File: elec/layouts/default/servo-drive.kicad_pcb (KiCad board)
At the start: 4 copper layers, 46 x 42.3 mm, 108 parts

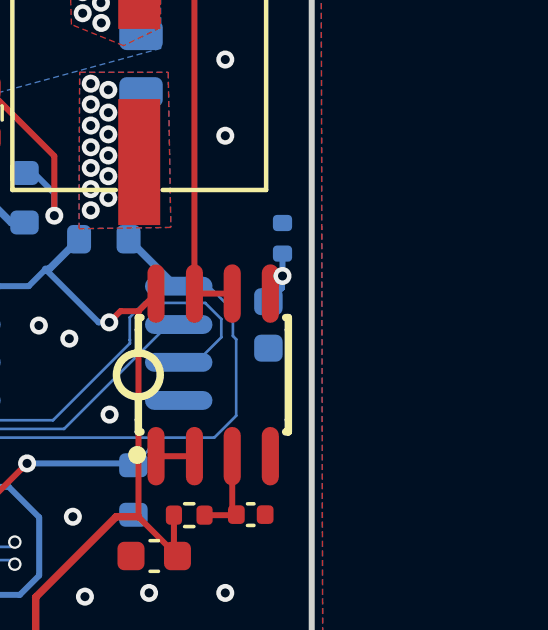
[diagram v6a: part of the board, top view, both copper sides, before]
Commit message: Upgrade default layout paths
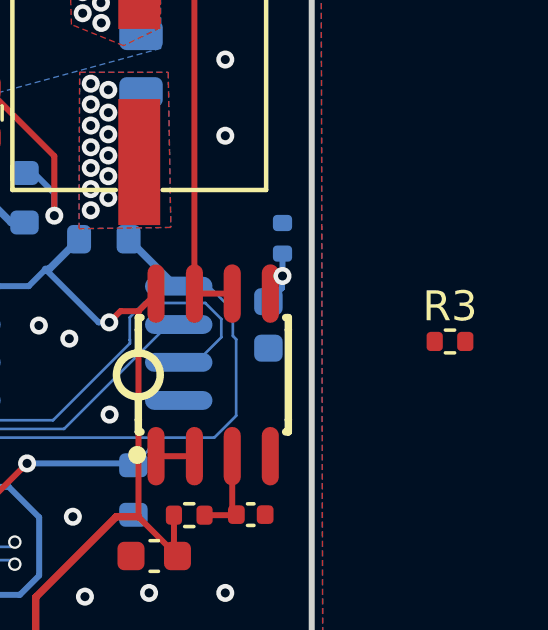
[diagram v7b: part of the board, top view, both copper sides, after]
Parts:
- added R3: 10kOhm, Resistor_SMD:R_0402_1005Metric, F.Cu at (177.7, 103.4)
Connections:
- net servo_drive.ato/ServoDrive.gnd renamed servo_drive.ato:ServoDrive.gnd
- net servo_drive.ato/ServoDrive.micro_kit/usb_dm-usb/dm renamed servo_drive.ato:ServoDrive.micro_kit.usb_dm-usb.dm
- net servo_drive.ato/ServoDrive.micro_kit/usb_dp-usb/dp renamed servo_drive.ato:ServoDrive.micro_kit.usb_dp-usb.dp
- net servo_drive.ato/ServoDrive.position_sensor/scl renamed servo_drive.ato:ServoDrive.position_sensor.scl
- net servo_drive.ato/ServoDrive.position_sensor/sda renamed servo_drive.ato:ServoDrive.position_sensor.sda
- net servo_drive.ato/ServoDrive.power_stage/high_in_a renamed servo_drive.ato:ServoDrive.power_stage.high_in_a
- net servo_drive.ato/ServoDrive.power_stage/high_in_b renamed servo_drive.ato:ServoDrive.power_stage.high_in_b
- net servo_drive.ato/ServoDrive.power_stage/high_in_c renamed servo_drive.ato:ServoDrive.power_stage.high_in_c
- net servo_drive.ato/ServoDrive.power_stage/i_fb_a renamed servo_drive.ato:ServoDrive.power_stage.i_fb_a
- net servo_drive.ato/ServoDrive.power_stage/i_fb_b renamed servo_drive.ato:ServoDrive.power_stage.i_fb_b
- net servo_drive.ato/ServoDrive.power_stage/i_fb_c renamed servo_drive.ato:ServoDrive.power_stage.i_fb_c
- net servo_drive.ato/ServoDrive.power_stage/low_in_a renamed servo_drive.ato:ServoDrive.power_stage.low_in_a
- net servo_drive.ato/ServoDrive.power_stage/low_in_b renamed servo_drive.ato:ServoDrive.power_stage.low_in_b
- net servo_drive.ato/ServoDrive.power_stage/low_in_c renamed servo_drive.ato:ServoDrive.power_stage.low_in_c
- net servo_drive.ato/ServoDrive.power_stage/out_a renamed servo_drive.ato:ServoDrive.power_stage.out_a
- net servo_drive.ato/ServoDrive.power_stage/out_b renamed servo_drive.ato:ServoDrive.power_stage.out_b
- net servo_drive.ato/ServoDrive.power_stage/out_c renamed servo_drive.ato:ServoDrive.power_stage.out_c
- net servo_drive.ato/ServoDrive.usb/cc1 renamed servo_drive.ato:ServoDrive.usb.cc1
- net servo_drive.ato/ServoDrive.usb/cc2 renamed servo_drive.ato:ServoDrive.usb.cc2
- net servo_drive.ato/ServoDrive.usb/vbus-usb_diode/anode renamed servo_drive.ato:ServoDrive.usb.vbus-usb_diode.anode
- net servo_drive.ato/ServoDrive.v_10 renamed servo_drive.ato:ServoDrive.v_10
- net servo_drive.ato/ServoDrive.v_3 renamed servo_drive.ato:ServoDrive.v_3
- net servo_drive.ato/ServoDrive.vbatt renamed servo_drive.ato:ServoDrive.vbatt
- net servo_drive.ato/ServoDrive.voltage_input_vdiv/out renamed servo_drive.ato:ServoDrive.voltage_input_vdiv.out
- net servo_drive.ato/ServoDrive/buck.SGND renamed servo_drive.ato:ServoDrive.buck.SGND
- net servo_drive.ato/ServoDrive/buck.buck_converter/BST renamed servo_drive.ato:ServoDrive.buck.buck_converter.BST
- net servo_drive.ato/ServoDrive/buck.buck_converter/FB-fb_vdiv/output renamed servo_drive.ato:ServoDrive.buck.buck_converter.FB-fb_vdiv.output
- net servo_drive.ato/ServoDrive/buck.buck_converter/LX renamed servo_drive.ato:ServoDrive.buck.buck_converter.LX
- net servo_drive.ato/ServoDrive/buck.buck_converter/SS renamed servo_drive.ato:ServoDrive.buck.buck_converter.SS
- net servo_drive.ato/ServoDrive/buck.buck_converter/VCC renamed servo_drive.ato:ServoDrive.buck.buck_converter.VCC
- net servo_drive.ato/ServoDrive/buck/buck_converter.CF renamed servo_drive.ato:ServoDrive.buck.buck_converter.CF
- net servo_drive.ato/ServoDrive/buck/buck_converter.RESET renamed servo_drive.ato:ServoDrive.buck.buck_converter.RESET
- net servo_drive.ato/ServoDrive/buck/buck_converter.RT renamed servo_drive.ato:ServoDrive.buck.buck_converter.RT
- net servo_drive.ato/ServoDrive/buck/buck_converter.SYNC renamed servo_drive.ato:ServoDrive.buck.buck_converter.SYNC
- net servo_drive.ato/ServoDrive/ldo.ldo_ic/bypass renamed servo_drive.ato:ServoDrive.ldo.ldo_ic.bypass
- net servo_drive.ato/ServoDrive/micro_kit.boot_vdiv/output-flash/ncs-micro/qspi_ss_n renamed servo_drive.ato:ServoDrive.micro_kit.boot_vdiv.output-flash.ncs-micro.qspi_ss_n
- net servo_drive.ato/ServoDrive/micro_kit.flash/clk-micro/qspi_sclk renamed servo_drive.ato:ServoDrive.micro_kit.flash.clk-micro.qspi_sclk
- net servo_drive.ato/ServoDrive/micro_kit.flash/di-micro/qspi_sd0 renamed servo_drive.ato:ServoDrive.micro_kit.flash.di-micro.qspi_sd0
- net servo_drive.ato/ServoDrive/micro_kit.flash/do-micro/qspi_sd1 renamed servo_drive.ato:ServoDrive.micro_kit.flash.do-micro.qspi_sd1
- net servo_drive.ato/ServoDrive/micro_kit.flash/io2-micro/qspi_sd2 renamed servo_drive.ato:ServoDrive.micro_kit.flash.io2-micro.qspi_sd2
- net servo_drive.ato/ServoDrive/micro_kit.flash/io3-micro/qspi_sd3 renamed servo_drive.ato:ServoDrive.micro_kit.flash.io3-micro.qspi_sd3
- net servo_drive.ato/ServoDrive/micro_kit.micro/dvdd-micro/vreg_vout renamed servo_drive.ato:ServoDrive.micro_kit.micro.dvdd-micro.vreg_vout
- net servo_drive.ato/ServoDrive/micro_kit.micro/run renamed servo_drive.ato:ServoDrive.micro_kit.micro.run
- net servo_drive.ato/ServoDrive/micro_kit.micro/usb_dm renamed servo_drive.ato:ServoDrive.micro_kit.micro.usb_dm
- net servo_drive.ato/ServoDrive/micro_kit.micro/usb_dp renamed servo_drive.ato:ServoDrive.micro_kit.micro.usb_dp
- net servo_drive.ato/ServoDrive/micro_kit.micro/xin-osc/in renamed servo_drive.ato:ServoDrive.micro_kit.micro.xin-osc.in
- net servo_drive.ato/ServoDrive/micro_kit.micro/xout renamed servo_drive.ato:ServoDrive.micro_kit.micro.xout
- net servo_drive.ato/ServoDrive/micro_kit.osc/out renamed servo_drive.ato:ServoDrive.micro_kit.osc.out
- net servo_drive.ato/ServoDrive/micro_kit/micro.gpio10 renamed servo_drive.ato:ServoDrive.micro_kit.micro.gpio10
- net servo_drive.ato/ServoDrive/micro_kit/micro.gpio11 renamed servo_drive.ato:ServoDrive.micro_kit.micro.gpio11
- net servo_drive.ato/ServoDrive/micro_kit/micro.gpio12 renamed servo_drive.ato:ServoDrive.micro_kit.micro.gpio12
- net servo_drive.ato/ServoDrive/micro_kit/micro.gpio13 renamed servo_drive.ato:ServoDrive.micro_kit.micro.gpio13
- net servo_drive.ato/ServoDrive/micro_kit/micro.gpio14 renamed servo_drive.ato:ServoDrive.micro_kit.micro.gpio14
- net servo_drive.ato/ServoDrive/micro_kit/micro.gpio15 renamed servo_drive.ato:ServoDrive.micro_kit.micro.gpio15
- net servo_drive.ato/ServoDrive/micro_kit/micro.gpio16 renamed servo_drive.ato:ServoDrive.micro_kit.micro.gpio16
- net servo_drive.ato/ServoDrive/micro_kit/micro.gpio17 renamed servo_drive.ato:ServoDrive.micro_kit.micro.gpio17
- net servo_drive.ato/ServoDrive/micro_kit/micro.gpio18 renamed servo_drive.ato:ServoDrive.micro_kit.micro.gpio18
- net servo_drive.ato/ServoDrive/micro_kit/micro.gpio19 renamed servo_drive.ato:ServoDrive.micro_kit.micro.gpio19
- net servo_drive.ato/ServoDrive/micro_kit/micro.gpio20 renamed servo_drive.ato:ServoDrive.micro_kit.micro.gpio20
- net servo_drive.ato/ServoDrive/micro_kit/micro.gpio21 renamed servo_drive.ato:ServoDrive.micro_kit.micro.gpio21
- net servo_drive.ato/ServoDrive/micro_kit/micro.gpio22 renamed servo_drive.ato:ServoDrive.micro_kit.micro.gpio22
- net servo_drive.ato/ServoDrive/micro_kit/micro.gpio23 renamed servo_drive.ato:ServoDrive.micro_kit.micro.gpio23
- net servo_drive.ato/ServoDrive/micro_kit/micro.gpio24 renamed servo_drive.ato:ServoDrive.micro_kit.micro.gpio24
- net servo_drive.ato/ServoDrive/micro_kit/micro.gpio25 renamed servo_drive.ato:ServoDrive.micro_kit.micro.gpio25
- net servo_drive.ato/ServoDrive/micro_kit/micro.gpio8 renamed servo_drive.ato:ServoDrive.micro_kit.micro.gpio8
- net servo_drive.ato/ServoDrive/micro_kit/micro.gpio9 renamed servo_drive.ato:ServoDrive.micro_kit.micro.gpio9
- net servo_drive.ato/ServoDrive/micro_kit/micro.iovdd renamed servo_drive.ato:ServoDrive.micro_kit.micro.iovdd
- net servo_drive.ato/ServoDrive/micro_kit/micro.swclk renamed servo_drive.ato:ServoDrive.micro_kit.micro.swclk
- net servo_drive.ato/ServoDrive/micro_kit/micro.swdio renamed servo_drive.ato:ServoDrive.micro_kit.micro.swdio
- net servo_drive.ato/ServoDrive/position_sensor.sensor/PGO renamed servo_drive.ato:ServoDrive.position_sensor.sensor.PGO
- net servo_drive.ato/ServoDrive/position_sensor/sensor.DIR renamed servo_drive.ato:ServoDrive.position_sensor.sensor.DIR
- net servo_drive.ato/ServoDrive/position_sensor/sensor.OUT renamed servo_drive.ato:ServoDrive.position_sensor.sensor.OUT
- net servo_drive.ato/ServoDrive/power_stage.current_sense_a/i_in-half_bridge_a/out renamed servo_drive.ato:ServoDrive.power_stage.current_sense_a.i_in-half_bridge_a.out
- net servo_drive.ato/ServoDrive/power_stage.current_sense_b/i_in-half_bridge_b/out renamed servo_drive.ato:ServoDrive.power_stage.current_sense_b.i_in-half_bridge_b.out
- net servo_drive.ato/ServoDrive/power_stage.current_sense_c/i_in-half_bridge_c/out renamed servo_drive.ato:ServoDrive.power_stage.current_sense_c.i_in-half_bridge_c.out
- net servo_drive.ato/ServoDrive/power_stage.half_v_ref renamed servo_drive.ato:ServoDrive.power_stage.half_v_ref
- net servo_drive.ato/ServoDrive/power_stage.v_ref renamed servo_drive.ato:ServoDrive.power_stage.v_ref
- net servo_drive.ato/ServoDrive/power_stage/current_sense_a.amp/in_n renamed servo_drive.ato:ServoDrive.power_stage.current_sense_a.amp.in_n
- net servo_drive.ato/ServoDrive/power_stage/current_sense_a.amp/in_p renamed servo_drive.ato:ServoDrive.power_stage.current_sense_a.amp.in_p
- net servo_drive.ato/ServoDrive/power_stage/current_sense_b.amp/in_n renamed servo_drive.ato:ServoDrive.power_stage.current_sense_b.amp.in_n
- net servo_drive.ato/ServoDrive/power_stage/current_sense_b.amp/in_p renamed servo_drive.ato:ServoDrive.power_stage.current_sense_b.amp.in_p
- net servo_drive.ato/ServoDrive/power_stage/current_sense_c.amp/in_n renamed servo_drive.ato:ServoDrive.power_stage.current_sense_c.amp.in_n
- net servo_drive.ato/ServoDrive/power_stage/current_sense_c.amp/in_p renamed servo_drive.ato:ServoDrive.power_stage.current_sense_c.amp.in_p
- net servo_drive.ato/ServoDrive/power_stage/half_bridge_a.gate_driver/hvg renamed servo_drive.ato:ServoDrive.power_stage.half_bridge_a.gate_driver.hvg
- net servo_drive.ato/ServoDrive/power_stage/half_bridge_a.gate_driver/lvg renamed servo_drive.ato:ServoDrive.power_stage.half_bridge_a.gate_driver.lvg
- net servo_drive.ato/ServoDrive/power_stage/half_bridge_a.gate_driver/vboot renamed servo_drive.ato:ServoDrive.power_stage.half_bridge_a.gate_driver.vboot
- net servo_drive.ato/ServoDrive/power_stage/half_bridge_a.hs_fet/gate renamed servo_drive.ato:ServoDrive.power_stage.half_bridge_a.hs_fet.gate
- net servo_drive.ato/ServoDrive/power_stage/half_bridge_a.ls_fet/gate renamed servo_drive.ato:ServoDrive.power_stage.half_bridge_a.ls_fet.gate
- net servo_drive.ato/ServoDrive/power_stage/half_bridge_b.gate_driver/hvg renamed servo_drive.ato:ServoDrive.power_stage.half_bridge_b.gate_driver.hvg
- net servo_drive.ato/ServoDrive/power_stage/half_bridge_b.gate_driver/lvg renamed servo_drive.ato:ServoDrive.power_stage.half_bridge_b.gate_driver.lvg
- net servo_drive.ato/ServoDrive/power_stage/half_bridge_b.gate_driver/vboot renamed servo_drive.ato:ServoDrive.power_stage.half_bridge_b.gate_driver.vboot
- net servo_drive.ato/ServoDrive/power_stage/half_bridge_b.hs_fet/gate renamed servo_drive.ato:ServoDrive.power_stage.half_bridge_b.hs_fet.gate
- net servo_drive.ato/ServoDrive/power_stage/half_bridge_b.ls_fet/gate renamed servo_drive.ato:ServoDrive.power_stage.half_bridge_b.ls_fet.gate
- net servo_drive.ato/ServoDrive/power_stage/half_bridge_c.gate_driver/hvg renamed servo_drive.ato:ServoDrive.power_stage.half_bridge_c.gate_driver.hvg
- net servo_drive.ato/ServoDrive/power_stage/half_bridge_c.gate_driver/lvg renamed servo_drive.ato:ServoDrive.power_stage.half_bridge_c.gate_driver.lvg
- net servo_drive.ato/ServoDrive/power_stage/half_bridge_c.gate_driver/vboot renamed servo_drive.ato:ServoDrive.power_stage.half_bridge_c.gate_driver.vboot
- net servo_drive.ato/ServoDrive/power_stage/half_bridge_c.hs_fet/gate renamed servo_drive.ato:ServoDrive.power_stage.half_bridge_c.hs_fet.gate
- net servo_drive.ato/ServoDrive/power_stage/half_bridge_c.ls_fet/gate renamed servo_drive.ato:ServoDrive.power_stage.half_bridge_c.ls_fet.gate
- net servo_drive.ato/ServoDrive/power_stage/ref.buffer/in_p_a-filter/out renamed servo_drive.ato:ServoDrive.power_stage.ref.buffer.in_p_a-filter.out
- net servo_drive.ato/ServoDrive/power_stage/ref.buffer/in_p_b-half_ref/output renamed servo_drive.ato:ServoDrive.power_stage.ref.buffer.in_p_b-half_ref.output
- net servo_drive.ato/ServoDrive/power_stage/ref/buffer.in_n_a-out_a renamed servo_drive.ato:ServoDrive.power_stage.ref.buffer.in_n_a-out_a
- net servo_drive.ato/ServoDrive/usb.sbu renamed servo_drive.ato:ServoDrive.usb.sbu

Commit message: routing complete
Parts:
- removed C20: 1uF, Capacitor_SMD:C_0805_2012Metric
- removed C36: 1uF, Capacitor_SMD:C_0603_1608Metric
- removed C37: 2.2uF, Capacitor_SMD:C_0603_1608Metric
- removed C38: 10nF, Capacitor_SMD:C_0603_1608Metric
- removed R12, R13, R5, R6: 10ohm, Resistor_SMD:R_0603_1608Metric
- removed R16: 1mOhm, Resistor_SMD:R_2512_6332Metric
- added R21: 18kOhm, Resistor_SMD:R_0603_1608Metric, B.Cu at (146.4, 105.4)
- added R22: , Resistor_SMD:R_0603_1608Metric, B.Cu at (146.4, 104.0)
- added U19: , lib:SC-70-6_L2.1-W1.3-P0.65-LS2.1-BR, B.Cu at (129.5, 105.8)
- added U22: , lib:SOT-23-5_L3.0-W1.7-P0.95-LS2.8-BL, B.Cu at (141.7, 111.3)
- added U23: , lib:SOT-23-5_L3.0-W1.7-P0.95-LS2.8-BL, B.Cu at (146.4, 108.1)
- C1, C2: value 1uF -> 100nF; footprint Capacitor_SMD:C_0402_1005Metric -> Capacitor_SMD:C_0603_1608Metric; moved to B.Cu
- C16, C19: footprint Capacitor_SMD:C_0805_2012Metric -> Capacitor_SMD:C_0603_1608Metric
- C18: footprint Capacitor_SMD:C_0805_2012Metric -> Capacitor_SMD:C_0603_1608Metric; moved to F.Cu
- C5: value (none) -> 1uF
- R1: value 10kOhm -> 100ohm; footprint Resistor_SMD:R_0402_1005Metric -> Resistor_SMD:R_0603_1608Metric; moved to B.Cu
- R17: value 10ohm -> 18kOhm
- R18: value 10ohm -> (none)
- R2: value 10kOhm -> 100ohm; footprint Resistor_SMD:R_0402_1005Metric -> Resistor_SMD:R_0603_1608Metric
- R3: value 10kOhm -> 10k; footprint Resistor_SMD:R_0402_1005Metric -> Resistor_SMD:R_0603_1608Metric
- R4, R8: value 1mOhm -> 3mOhm; footprint Resistor_SMD:R_2512_6332Metric -> Resistor_SMD:R_2010_5025Metric
- U1, U4: footprint lib:VSSOP-8_L3.0-W3.0-P0.65-LS5.0-BL -> lib:SOIC-8_L5.0-W4.0-P1.27-LS6.0-BL
- U11: footprint lib:SOT-23-5_L3.0-W1.7-P0.95-LS2.8-BR -> lib:KEY-SMD_SKTDLDE010
- U17: footprint lib:SOIC-8_L5.0-W4.0-P1.27-LS6.0-BL -> lib:CONN-SMD_4P-P1.00_SM04B-SRSS-TB-LF-SN
- U5: footprint lib:VSSOP-8_L3.0-W3.0-P0.65-LS5.0-BL -> lib:LED-SMD_4P-L4.0-W1.4_SK6805SIDE-S; moved to F.Cu
- moved R1 39.9 mm to (140.4, 81.3), turned to 90 degrees
- moved U17 39.8 mm to (130.0, 105.7), turned to -90 degrees
- moved C5 39.5 mm to (132.3, 107.1), turned to 180 degrees
- moved C2 32.5 mm to (149.0, 85.2), turned to 90 degrees
- moved R18 31.5 mm to (141.6, 107.0), turned to 0 degrees
- moved R17 29.9 mm to (141.6, 108.5)
- moved R2 29.2 mm to (149.0, 82.1), turned to 90 degrees
- moved C1 28.3 mm to (140.4, 84.3), turned to 90 degrees
- moved U5 27.5 mm to (171.8, 108.0), turned to 90 degrees
- moved C16 26.3 mm to (143.8, 110.7), turned to -90 degrees
- moved C18 25.6 mm to (169.4, 106.4)
- moved U11 23.1 mm to (171.5, 102.6), turned to -90 degrees
- moved C13 11.2 mm to (159.2, 84.0), turned to 90 degrees
- moved R3 9.38 mm to (168.3, 103.1)
- moved C19 6.17 mm to (161.0, 84.0), turned to 90 degrees
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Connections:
- C1 pad 1: servo_drive.ato:ServoDrive.v_3 -> servo_drive.ato:ServoDrive.gnd
- C1 pad 2: servo_drive.ato:ServoDrive.gnd -> servo_drive.ato:ServoDrive.power_stage.i_fb_a
- C16 pad 1: servo_drive.ato:ServoDrive.power_stage.current_sense_a.amp.in_p -> servo_drive.ato:ServoDrive.v_5
- C16 pad 2: servo_drive.ato:ServoDrive.power_stage.current_sense_a.amp.in_n -> servo_drive.ato:ServoDrive.gnd
- C18 pad 1: servo_drive.ato:ServoDrive.power_stage.current_sense_b.amp.in_p -> servo_drive.ato:ServoDrive.v_5
- C18 pad 2: servo_drive.ato:ServoDrive.power_stage.current_sense_b.amp.in_n -> servo_drive.ato:ServoDrive.gnd
- C2 pad 1: servo_drive.ato:ServoDrive.power_stage.ref.buffer.in_p_a-filter.out -> servo_drive.ato:ServoDrive.gnd
- C2 pad 2: servo_drive.ato:ServoDrive.gnd -> servo_drive.ato:ServoDrive.power_stage.i_fb_b
- C45 pad 2: servo_drive.ato:ServoDrive.power_stage.current_sense_c.i_in-half_bridge_c.out -> servo_drive.ato:ServoDrive.power_stage.out_c
- C5 pad 1: servo_drive.ato:ServoDrive.power_stage.ref.buffer.in_p_b-half_ref.output -> servo_drive.ato:ServoDrive.v_10
- D1 pad 1: servo_drive.ato:ServoDrive.v_10 -> servo_drive.ato:ServoDrive.v_5
- Q5 pad 1: servo_drive.ato:ServoDrive.power_stage.current_sense_c.i_in-half_bridge_c.out -> servo_drive.ato:ServoDrive.power_stage.out_c
- Q5 pad 2: servo_drive.ato:ServoDrive.power_stage.current_sense_c.i_in-half_bridge_c.out -> servo_drive.ato:ServoDrive.power_stage.out_c
- Q5 pad 3: servo_drive.ato:ServoDrive.power_stage.current_sense_c.i_in-half_bridge_c.out -> servo_drive.ato:ServoDrive.power_stage.out_c
- Q6 pad 5: servo_drive.ato:ServoDrive.power_stage.current_sense_c.i_in-half_bridge_c.out -> servo_drive.ato:ServoDrive.power_stage.out_c
- Q6 pad 6: servo_drive.ato:ServoDrive.power_stage.current_sense_c.i_in-half_bridge_c.out -> servo_drive.ato:ServoDrive.power_stage.out_c
- Q6 pad 7: servo_drive.ato:ServoDrive.power_stage.current_sense_c.i_in-half_bridge_c.out -> servo_drive.ato:ServoDrive.power_stage.out_c
- Q6 pad 8: servo_drive.ato:ServoDrive.power_stage.current_sense_c.i_in-half_bridge_c.out -> servo_drive.ato:ServoDrive.power_stage.out_c
- Q6 pad 9: servo_drive.ato:ServoDrive.power_stage.current_sense_c.i_in-half_bridge_c.out -> servo_drive.ato:ServoDrive.power_stage.out_c
- R1 pad 1: servo_drive.ato:ServoDrive.v_3 -> servo_drive.ato:ServoDrive.power_stage.i_fb_a
- R1 pad 2: servo_drive.ato:ServoDrive.power_stage.ref.buffer.in_p_a-filter.out -> servo_drive.ato:ServoDrive.power_stage.current_sense_a.amp.out
- R17 pad 1: servo_drive.ato:ServoDrive.power_stage.current_sense_c.i_in-half_bridge_c.out -> servo_drive.ato:ServoDrive.v_5
- R17 pad 2: servo_drive.ato:ServoDrive.power_stage.current_sense_c.amp.in_p -> servo_drive.ato:ServoDrive.ldo_5v.feedback_div.output-ldo.adj
- R18 pad 1: servo_drive.ato:ServoDrive.power_stage.out_c -> servo_drive.ato:ServoDrive.ldo_5v.feedback_div.output-ldo.adj
- R18 pad 2: servo_drive.ato:ServoDrive.power_stage.current_sense_c.amp.in_n -> servo_drive.ato:ServoDrive.gnd
- R2 pad 1: servo_drive.ato:ServoDrive.power_stage.v_ref -> servo_drive.ato:ServoDrive.power_stage.i_fb_b
- R2 pad 2: servo_drive.ato:ServoDrive.power_stage.ref.buffer.in_p_b-half_ref.output -> servo_drive.ato:ServoDrive.power_stage.current_sense_b.amp.out
- R3 pad 1: servo_drive.ato:ServoDrive.power_stage.ref.buffer.in_p_b-half_ref.output -> servo_drive.ato:ServoDrive.gnd
- R3 pad 2: servo_drive.ato:ServoDrive.gnd -> servo_drive.ato:ServoDrive.switch.pin1
- R42 pad 2: servo_drive.ato:ServoDrive.power_stage.current_sense_c.i_in-half_bridge_c.out -> servo_drive.ato:ServoDrive.power_stage.out_c
- U1 pad 1: servo_drive.ato:ServoDrive.power_stage.current_sense_a.amp.in_p -> servo_drive.ato:ServoDrive.power_stage.current_sense_a.i_in-half_bridge_a.out
- U1 pad 3: servo_drive.ato:ServoDrive.v_3 -> servo_drive.ato:ServoDrive.gnd
- U1 pad 4: servo_drive.ato:ServoDrive.power_stage.i_fb_a -> servo_drive.ato:ServoDrive.power_stage.current_sense_a.amp.NC
- U1 pad 5: servo_drive.ato:ServoDrive.gnd -> servo_drive.ato:ServoDrive.power_stage.current_sense_a.amp.out
- U1 pad 7: servo_drive.ato:ServoDrive.power_stage.half_v_ref -> servo_drive.ato:ServoDrive.v_3
- U1 pad 8: servo_drive.ato:ServoDrive.power_stage.current_sense_a.amp.in_n -> servo_drive.ato:ServoDrive.power_stage.out_a
- U11 pad 1: servo_drive.ato:ServoDrive.v_10 -> servo_drive.ato:ServoDrive.switch.pin1
- U11 pad 2: servo_drive.ato:ServoDrive.gnd -> servo_drive.ato:ServoDrive.v_3
- U11 pad 3: servo_drive.ato:ServoDrive.v_10 -> (no net)
- U11 pad 4: servo_drive.ato:ServoDrive.ldo.ldo_ic.bypass -> (no net)
- U15 pad 13: servo_drive.ato:ServoDrive.micro_kit.micro.gpio10 -> servo_drive.ato:ServoDrive.i2c_active_terminator.bus1-stemma.sda
- U15 pad 14: servo_drive.ato:ServoDrive.micro_kit.micro.gpio11 -> servo_drive.ato:ServoDrive.i2c_active_terminator.bus2-stemma.scl
- U15 pad 36: servo_drive.ato:ServoDrive.micro_kit.micro.gpio24 -> servo_drive.ato:ServoDrive.switch.pin1
- U15 pad 37: servo_drive.ato:ServoDrive.micro_kit.micro.gpio25 -> servo_drive.ato:ServoDrive.led.data_in
- U15 pad 40: servo_drive.ato:ServoDrive.power_stage.i_fb_c -> servo_drive.ato:ServoDrive.micro_kit.micro.gpio28_a2
- U16 pad 6: servo_drive.ato:ServoDrive.power_stage.current_sense_c.i_in-half_bridge_c.out -> servo_drive.ato:ServoDrive.power_stage.out_c
- U17 pad 1: servo_drive.ato:ServoDrive.power_stage.ref.buffer.in_n_a-out_a -> servo_drive.ato:ServoDrive.gnd
- U17 pad 2: servo_drive.ato:ServoDrive.power_stage.ref.buffer.in_n_a-out_a -> servo_drive.ato:ServoDrive.v_3
- U17 pad 3: servo_drive.ato:ServoDrive.power_stage.ref.buffer.in_p_a-filter.out -> servo_drive.ato:ServoDrive.i2c_active_terminator.bus1-stemma.sda
- U17 pad 4: servo_drive.ato:ServoDrive.gnd -> servo_drive.ato:ServoDrive.i2c_active_terminator.bus2-stemma.scl
- U17 pad 5: servo_drive.ato:ServoDrive.power_stage.ref.buffer.in_p_b-half_ref.output -> (no net)
- U17 pad 6: servo_drive.ato:ServoDrive.power_stage.half_v_ref -> (no net)
- U4 pad 1: servo_drive.ato:ServoDrive.power_stage.current_sense_b.amp.in_p -> servo_drive.ato:ServoDrive.power_stage.current_sense_b.i_in-half_bridge_b.out
- U4 pad 3: servo_drive.ato:ServoDrive.v_3 -> servo_drive.ato:ServoDrive.gnd
- U4 pad 4: servo_drive.ato:ServoDrive.power_stage.i_fb_b -> servo_drive.ato:ServoDrive.power_stage.current_sense_b.amp.NC
- U4 pad 5: servo_drive.ato:ServoDrive.gnd -> servo_drive.ato:ServoDrive.power_stage.current_sense_b.amp.out
- U4 pad 7: servo_drive.ato:ServoDrive.power_stage.half_v_ref -> servo_drive.ato:ServoDrive.v_3
- U4 pad 8: servo_drive.ato:ServoDrive.power_stage.current_sense_b.amp.in_n -> servo_drive.ato:ServoDrive.power_stage.out_b
- U5 pad 1: servo_drive.ato:ServoDrive.power_stage.current_sense_c.amp.in_p -> servo_drive.ato:ServoDrive.v_5
- U5 pad 3: servo_drive.ato:ServoDrive.v_3 -> servo_drive.ato:ServoDrive.led.data_out
- U5 pad 4: servo_drive.ato:ServoDrive.power_stage.i_fb_c -> servo_drive.ato:ServoDrive.led.data_in
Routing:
- net servo_drive.ato:ServoDrive.power_stage.half_v_ref: track 46.2 -> 0.00 mm, vias 3 -> 0
- net servo_drive.ato:ServoDrive.i2c_active_terminator.bus2-stemma.scl: track 0.00 -> 44.0 mm, vias 0 -> 2
- net servo_drive.ato:ServoDrive.i2c_active_terminator.bus1-stemma.sda: track 0.00 -> 43.1 mm, vias 0 -> 2
- net servo_drive.ato:ServoDrive.v_5: track 0.00 -> 39.3 mm, vias 0 -> 3
- net servo_drive.ato:ServoDrive.power_stage.i_fb_c: track 33.6 -> 0.00 mm, vias 3 -> 0
- net servo_drive.ato:ServoDrive.switch.pin1: track 0.00 -> 33.2 mm, vias 0 -> 2
- net servo_drive.ato:ServoDrive.power_stage.current_sense_c.i_in-half_bridge_c.out: track 30.0 -> 0.00 mm, vias 10 -> 0
- net servo_drive.ato:ServoDrive.led.data_in: track 0.00 -> 23.2 mm, vias 0 -> 1
- net servo_drive.ato:ServoDrive.power_stage.out_c: track 4.24 -> 26.4 mm, vias 0 -> 10
- net servo_drive.ato:ServoDrive.micro_kit.micro.gpio28_a2: track 0.00 -> 10.4 mm, vias 0 -> 1
- net servo_drive.ato:ServoDrive.v_3: track 161.9 -> 169.8 mm
- net servo_drive.ato:ServoDrive.power_stage.current_sense_b.amp.in_n: track 7.32 -> 0.00 mm
- net servo_drive.ato:ServoDrive.power_stage.current_sense_b.amp.in_p: track 4.85 -> 0.00 mm
- net servo_drive.ato:ServoDrive.power_stage.current_sense_a.amp.in_p: track 4.50 -> 0.00 mm
- net servo_drive.ato:ServoDrive.power_stage.current_sense_c.amp.in_p: track 4.48 -> 0.00 mm
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- added copper zone on B.Cu, net servo_drive.ato:ServoDrive.power_stage.out_c
- removed copper zone on B.Cu, net servo_drive.ato:ServoDrive.power_stage.current_sense_c.i_in-half_bridge_c.out
- removed copper zone on F.Cu, net servo_drive.ato:ServoDrive.power_stage.current_sense_c.i_in-half_bridge_c.out
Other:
- outline, holes or cut-outs redrawn
